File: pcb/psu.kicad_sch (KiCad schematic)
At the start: 32 parts, among them J1 PZ254V-11-02P, U1 TPS5430DDAR, U11 AMS1117-3.3, U4 DC-005H-D020, U5 15uH

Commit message: hardware: correct 3.3 V regulator ordering data
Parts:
- U11: LCSC Part C6187 -> C6186; MPN AMS1117-5.0 -> AMS1117-3.3
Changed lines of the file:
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@@
 			)
 		)
-		(property "MPN" "AMS1117-5.0"
+		(property "MPN" "AMS1117-3.3"
 			(at 162.56 157.48 0)
 			(hide yes)
@@
 			)
 		)
-		(property "LCSC Part" "C6187"
+		(property "LCSC Part" "C6186"
 			(at 162.56 160.02 0)
 			(hide yes)

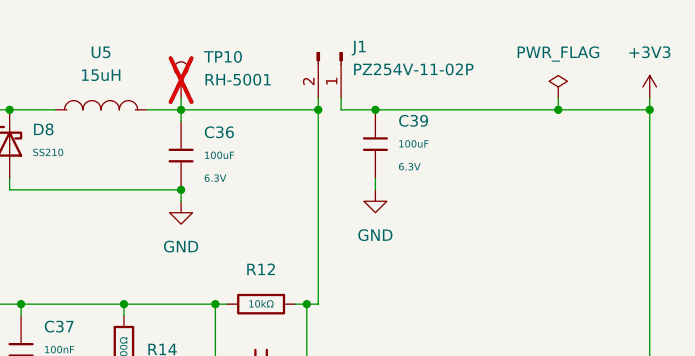
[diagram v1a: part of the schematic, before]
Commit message: sch: remove 3.3v jumper
Fixes #16
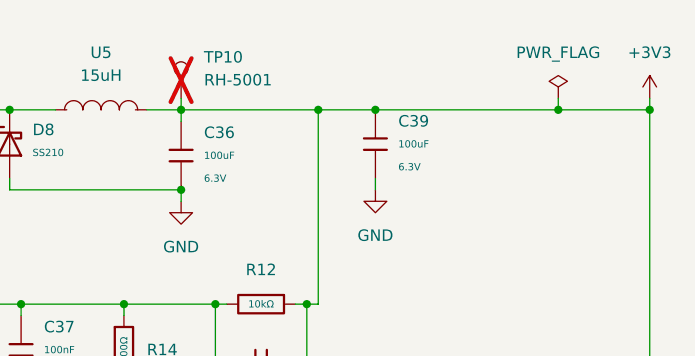
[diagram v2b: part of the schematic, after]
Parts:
- removed J1: PZ254V-11-02P, EasyEDA:HDR-TH_2P-P2.54-V-M, symbol Connector:Conn_01x02_Pin
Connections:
- net +3V3: now also C36.1, C8.1, R12.1, TP10.1, U5.2
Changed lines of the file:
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@@
 	)
 	(junction
-		(at 208.28 52.07)
-		(diameter 0)
-		(color 0 0 0 0)
-	)
-	(junction
 		(at 76.2 62.23)
 		(diameter 0)
@@
 	)
 	(junction
+		(at 208.28 52.07)
+		(diameter 0)
+		(color 0 0 0 0)
+	)
+	(junction
 		(at 97.79 52.07)
 		(diameter 0)
@@
 	(wire
 		(pts
-			(xy 210.82 52.07) (xy 214.63 52.07)
-		)
-		(stroke
-			(width 0)
-			(type default)
-		)
-	)
-	(wire
-		(pts
 			(xy 139.7 138.43) (xy 151.13 138.43)
 		)
@@
 	(wire
 		(pts
-			(xy 208.28 52.07) (xy 208.28 50.8)
-		)
-		(stroke
-			(width 0)
-			(type default)
-		)
-	)
-	(wire
-		(pts
 			(xy 234.95 52.07) (xy 245.11 52.07)
 		)
@@
 	(wire
 		(pts
-			(xy 214.63 59.69) (xy 214.63 60.96)
+			(xy 208.28 52.07) (xy 214.63 52.07)
 		)
 		(stroke
@@
 	(wire
 		(pts
-			(xy 198.12 80.01) (xy 196.85 80.01)
+			(xy 214.63 59.69) (xy 214.63 60.96)
 		)
 		(stroke
@@
 	(wire
 		(pts
-			(xy 193.04 52.07) (xy 193.04 53.34)
+			(xy 198.12 80.01) (xy 196.85 80.01)
 		)
 		(stroke
@@
 	(wire
 		(pts
-			(xy 210.82 50.8) (xy 210.82 52.07)
+			(xy 193.04 52.07) (xy 193.04 53.34)
 		)
 		(stroke
@@
 					(unit 1)
 				)
-			)
-		)
-	)
-	(symbol
-		(lib_id "Connector:Conn_01x02_Pin")
-		(at 210.82 45.72 270)
-		(unit 1)
-		(body_style 1)
-		(exclude_from_sim no)
-		(in_bom yes)
-		(on_board yes)
-		(in_pos_files yes)
-		(dnp no)
-		(fields_autoplaced yes)
-		(property "Reference" "J1"
-			(at 212.09 45.0849 90)
-			(show_name no)
-			(do_not_autoplace no)
-			(effects
-				(font
-					(size 1.27 1.27)
-				)
-				(justify left)
-			)
-		)
-		(property "Value" "PZ254V-11-02P"
-			(at 212.09 47.6249 90)
-			(show_name no)
-			(do_not_autoplace no)
-			(effects
-				(font
-					(size 1.27 1.27)
-				)
-				(justify left)
-			)
-		)
-		(property "Footprint" "EasyEDA:HDR-TH_2P-P2.54-V-M"
-			(at 210.82 45.72 0)
-			(hide yes)
-			(show_name no)
-			(do_not_autoplace no)
-			(effects
-				(font
-					(size 1.27 1.27)
-				)
-			)
-		)
-		(property "Datasheet" ""
-			(at 210.82 45.72 0)
-			(hide yes)
-			(show_name no)
-			(do_not_autoplace no)
-			(effects
-				(font
-					(size 1.27 1.27)
-				)
-			)
-		)
-		(property "Description" "3V3_JMP"
-			(at 210.82 45.72 0)
-			(hide yes)
-			(show_name no)
-			(do_not_autoplace no)
-			(effects
-				(font
-					(size 1.27 1.27)
-				)
-			)
-		)
-		(property "LSCS Part" "C492401"
-			(at 210.82 45.72 90)
-			(hide yes)
-			(show_name no)
-			(do_not_autoplace no)
-			(effects
-				(font
-					(size 1.27 1.27)
-				)
-			)
-		)
-		(property "MPN" "PZ254V-11-02P"
-			(at 210.82 45.72 90)
-			(hide yes)
-			(show_name no)
-			(do_not_autoplace no)
-			(effects
-				(font
-					(size 1.27 1.27)
-				)
-			)
-		)
-		(property "Sim.Pins" ""
-			(at 210.82 45.72 90)
-			(hide yes)
-			(show_name no)
-			(do_not_autoplace no)
-			(effects
-				(font
-					(size 1.27 1.27)
-				)
-			)
-		)
-		(property "KLC_S3.3" ""
-			(at 210.82 45.72 90)
-			(hide yes)
-			(show_name no)
-			(do_not_autoplace no)
-			(effects
-				(font
-					(size 1.27 1.27)
-				)
-			)
-		)
-		(property "KLC_S4.1" ""
-			(at 210.82 45.72 90)
-			(hide yes)
-			(show_name no)
-			(do_not_autoplace no)
-			(effects
-				(font
-					(size 1.27 1.27)
-				)
-			)
-		)
-		(pin "2"
-		)
-		(pin "1"
-		)
-		(instances
-			(project "EveningStar"
-				(path "/4c61f5a2-f8d4-462a-9bc3-d74437d30372/2e538fbd-4766-4d3c-804f-b602af6e3385"
-					(reference "J1")
-					(unit 1)
-				)

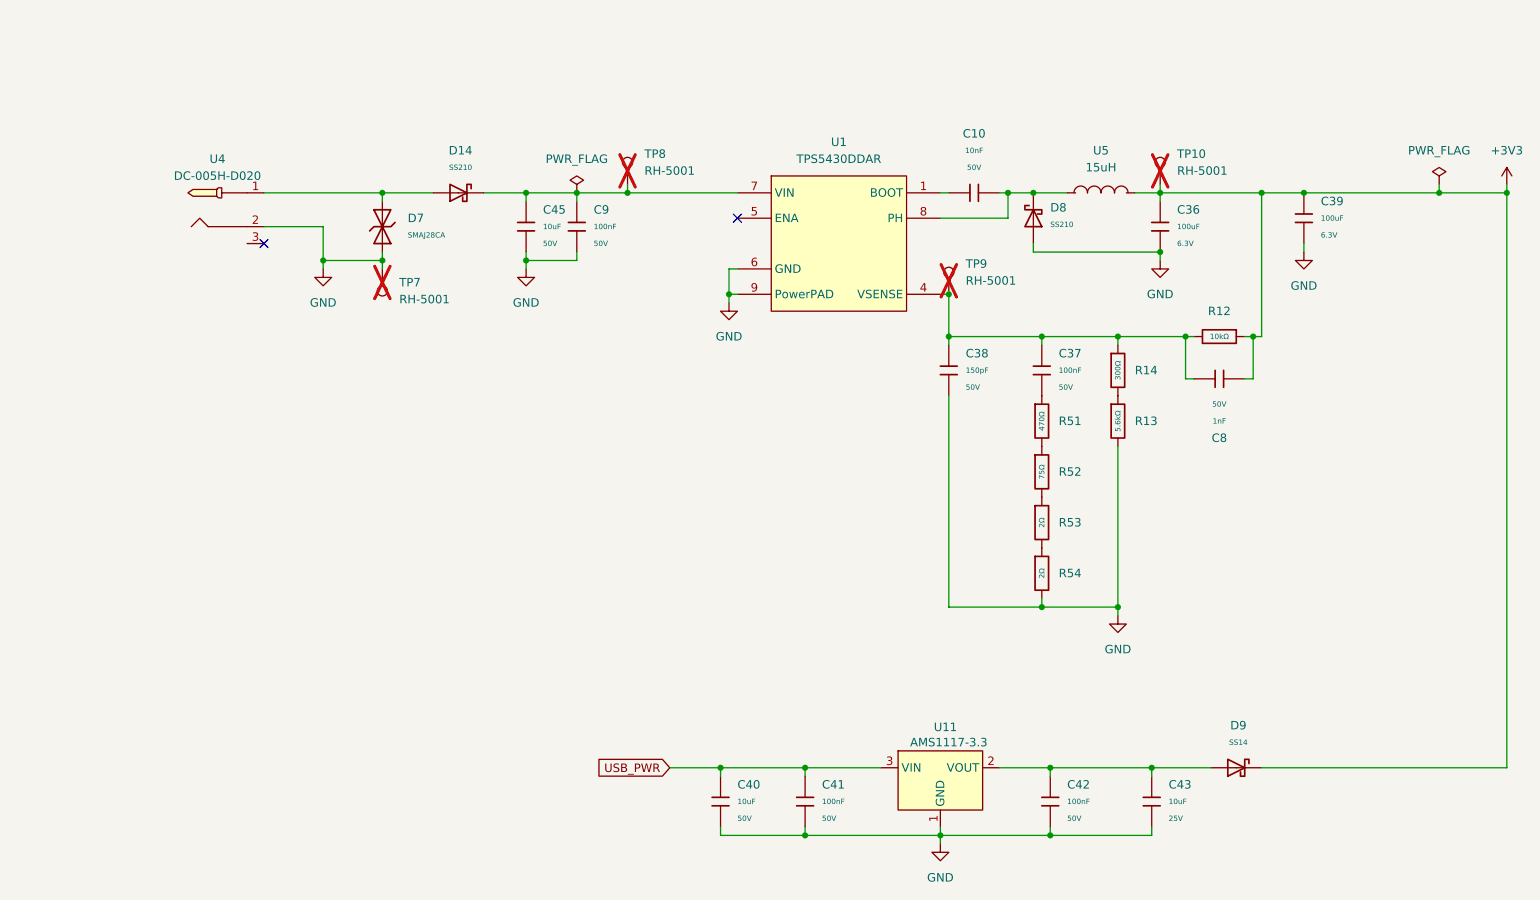
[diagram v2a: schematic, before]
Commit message: sch: remove usb power and clean up mcu sheet
Fixes #15
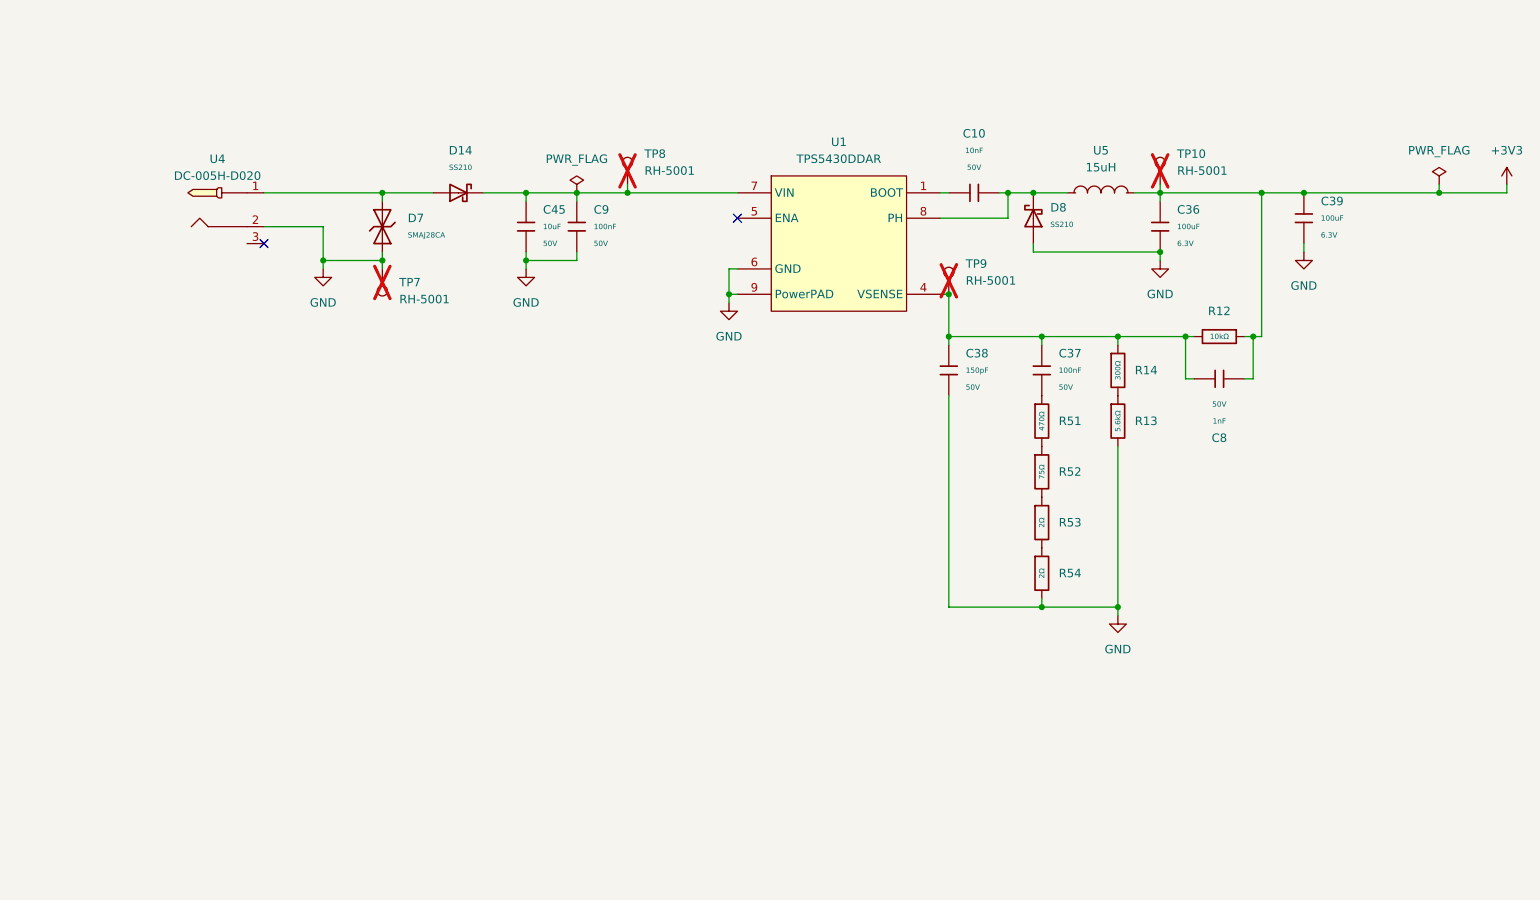
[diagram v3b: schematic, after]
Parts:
- removed C40: 10uF, PCM_JLCPCB:C_1206, symbol PCM_JLCPCB-Capacitors:1206,10uF
- removed C41, C42: 100nF, PCM_JLCPCB:C_0603, symbol PCM_JLCPCB-Capacitors:0603,100nF
- removed C43: 10uF, PCM_JLCPCB:C_0603, symbol PCM_JLCPCB-Capacitors:0603,10uF,(2)
- removed D9: SS14, PCM_JLCPCB:D_SMA, symbol PCM_JLCPCB-Diodes:Schottky,SS14
- removed U11: AMS1117-3.3, EasyEDA:SOT-223_L6.5-W3.5-P2.30-LS7.0-BR, symbol EasyEDA:AMS1117-5.0

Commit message: sch: replace power supply IC with LMR38020S and use screw terminals
This DC-DC IC is a better fit for the maximum voltages of a 24VDC
lead-acid battery system, and allows plenty of headroom for appropriate
TVS diode selection. Fixes #53

Also replaces the DC barrel jack with pluggable screw terminals. Fixes
#30
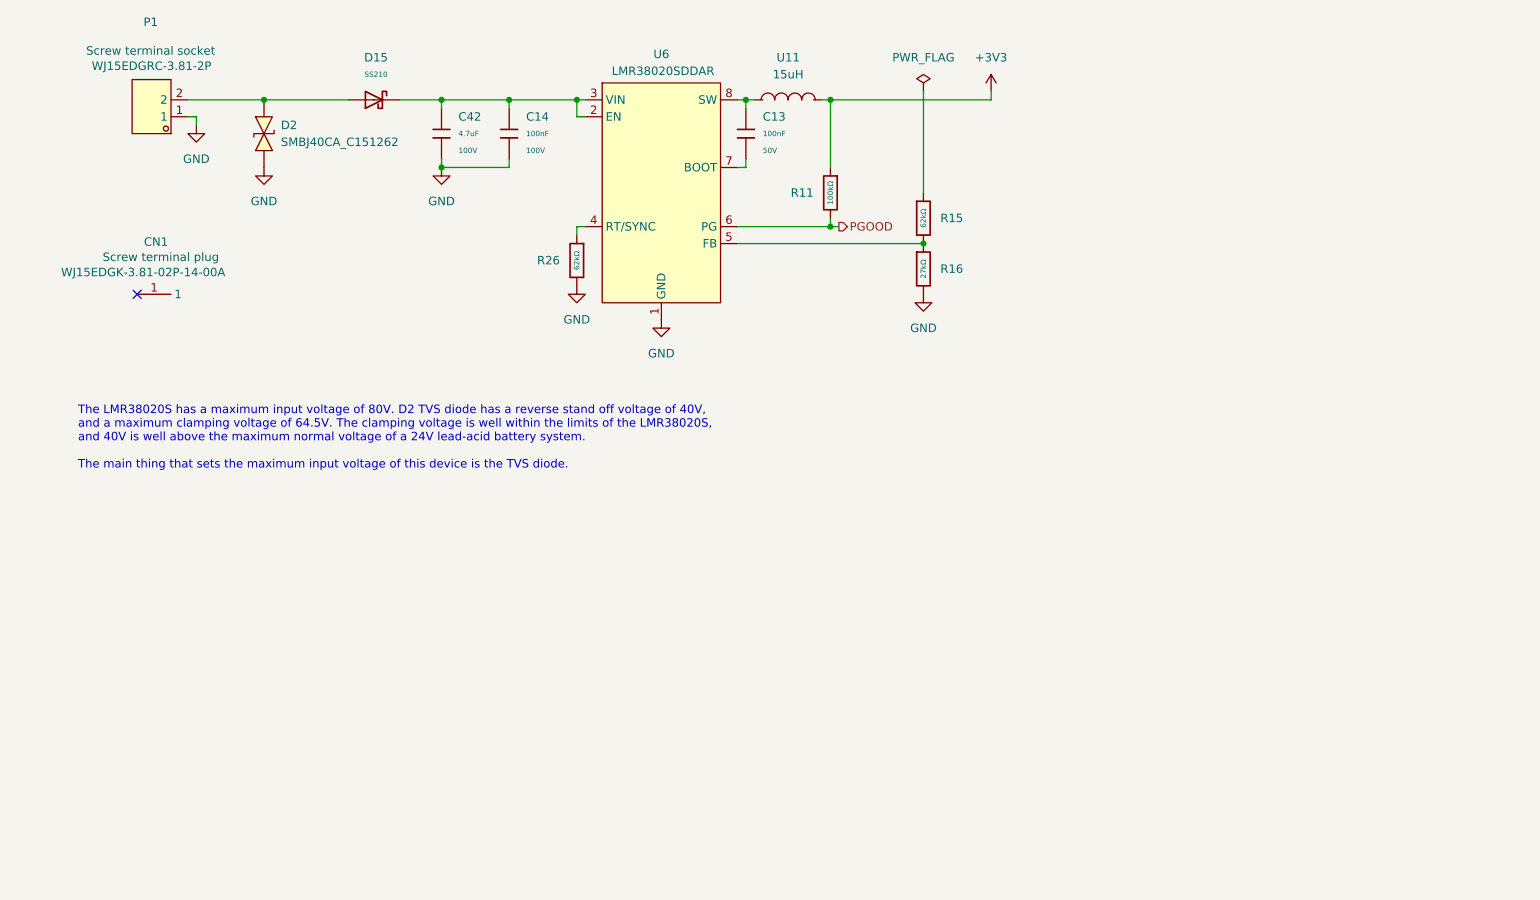
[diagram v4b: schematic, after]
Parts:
- removed C10: 10nF, PCM_JLCPCB:C_0603, symbol PCM_JLCPCB-Capacitors:0603,10nF
- removed C36, C39: 100uF, PCM_JLCPCB:C_1206, symbol PCM_JLCPCB-Capacitors:1206,100uF
- removed C37, C9: 100nF, PCM_JLCPCB:C_0603, symbol PCM_JLCPCB-Capacitors:0603,100nF
- removed C38: 150pF, PCM_JLCPCB:C_0603, symbol PCM_JLCPCB-Capacitors:0603,150pF
- removed C45: 10uF, PCM_JLCPCB:C_0805, symbol PCM_JLCPCB-Capacitors:0805,10uF,(2)
- removed C8: 1nF, PCM_JLCPCB:C_0603, symbol PCM_JLCPCB-Capacitors:0603,1nF
- removed D14, D8: SS210, PCM_JLCPCB:D_SMA, symbol PCM_JLCPCB-Diodes:Schottky,SS210
- removed D7: SMAJ28CA, PCM_JLCPCB:D_DO-214AC(SMA), symbol PCM_JLCPCB-Diodes:TVS-Bi,SMAJ28CA
- removed R12: 10kΩ, PCM_JLCPCB:R_0603, symbol PCM_JLCPCB-Resistors:0603,10kΩ
- removed R13: 5.6kΩ, PCM_JLCPCB:R_0603, symbol PCM_JLCPCB-Resistors:0603,5.6kΩ
- removed R14: 300Ω, PCM_JLCPCB:R_0603, symbol PCM_JLCPCB-Resistors:0603,300Ω
- removed R51: 470Ω, PCM_JLCPCB:R_0603, symbol PCM_JLCPCB-Resistors:0603,470Ω
- removed R52: 75Ω, PCM_JLCPCB:R_0603, symbol PCM_JLCPCB-Resistors:0603,75Ω
- removed R53, R54: 2Ω, PCM_JLCPCB:R_0603, symbol PCM_JLCPCB-Resistors:0603,2Ω
- removed TP10, TP7, TP8, TP9: RH-5001, EasyEDA:TEST-TH_BD2.54-P1.4_BLACK, symbol Connector:TestPoint
- removed U1: TPS5430DDAR, EasyEDA:ESOP-8_L4.9-W3.9-P1.27-LS6.0-TL-EP, symbol EasyEDA:TPS5430DDAR
- removed U4: DC-005H-D020, EasyEDA:DC-IN-TH_G-SWITCH_DC-005H-D020, symbol EasyEDA:DC-005H-D020
- removed U5: 15uH, EasyEDA:IND-SMD_L7.1-W6.6, symbol EasyEDA:APH0630T150M
- added C13: 100nF, PCM_JLCPCB:C_0603, symbol PCM_JLCPCB-Capacitors:0603,100nF
- added C14: 100nF, PCM_JLCPCB:C_0805, symbol PCM_JLCPCB-Capacitors:0805,100nF
- added C42: 4.7uF, PCM_JLCPCB:C_1206, symbol PCM_JLCPCB-Capacitors:0805,100nF
- added CN1: WJ15EDGK-3.81-02P-14-00A, EasyEDA:FL_001, symbol EasyEDA:WJ15EDGK-3.81-02P-14-00A
- added D15: SS210, PCM_JLCPCB:D_SMA, symbol PCM_JLCPCB-Diodes:Schottky,SS210
- added D2: SMBJ40CA_C151262, EasyEDA:SMB_L4.6-W3.6-LS5.3-BI, symbol EasyEDA:SMBJ40CA_C151262
- added P1: WJ15EDGRC-3.81-2P, EasyEDA:CONN-TH_2P-P3.81_WJ15EDGRC-3.81-2P, symbol EasyEDA:WJ15EDGRC-3.81-2P
- added R11: 100kΩ, PCM_JLCPCB:R_0603, symbol PCM_JLCPCB-Resistors:0603,100kΩ
- added R15, R26: 62kΩ, PCM_JLCPCB:R_0603, symbol PCM_JLCPCB-Resistors:0603,62kΩ
- added R16: 27kΩ, PCM_JLCPCB:R_0603, symbol PCM_JLCPCB-Resistors:0603,27kΩ
- added U11: 15uH, EasyEDA:IND-SMD_L7.1-W6.6, symbol EasyEDA:APH0630T150M
- added U6: LMR38020SDDAR, EasyEDA:ESOP-8_L4.9-W3.9-P1.27-LS6.0-BL-EP-1, symbol EasyEDA:LMR38020SDDAR
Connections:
- net +3V3: now also R11.1, U11.2
- net GND: now also C14.2, C42.2, D2.1 (K), P1.1, R16.2, R26.2, U6.1 (GND)
- new net: R26.1, U6.4 (RT/SYNC)
- new net: C14.1, C42.1, D15.1, U6.2 (EN), U6.3 (VIN)
- new net: C13.1, U11.1, U6.8 (SW)
- new net: D15.2, D2.2 (A), P1.2
- new net: C13.2, U6.7 (BOOT)
- new net: R15.2, R16.1, U6.5 (FB)
- new net PGOOD: R11.2, U6.6 (PG)
- no-connect marks 2 -> 1
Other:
- note added: "The LMR38020S has a maximum input voltage of 80V. D2 TVS diode has a reverse stand off voltage of 40V, and a maximum clamping voltage of 64.5V. The clamping voltage is well within the limits of the LMR38020S, and 40V is well above the maximum normal voltage of a 24V lead-acid battery system. The main thing that sets the maximum input voltage of this device is the TVS diode."
